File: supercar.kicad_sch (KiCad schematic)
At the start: 41 parts, among them SW1 Power, U1 74HC283, U2 74HC574, U3 74HC154, U4 74HC574, U5 74HC86, U6 NE555D

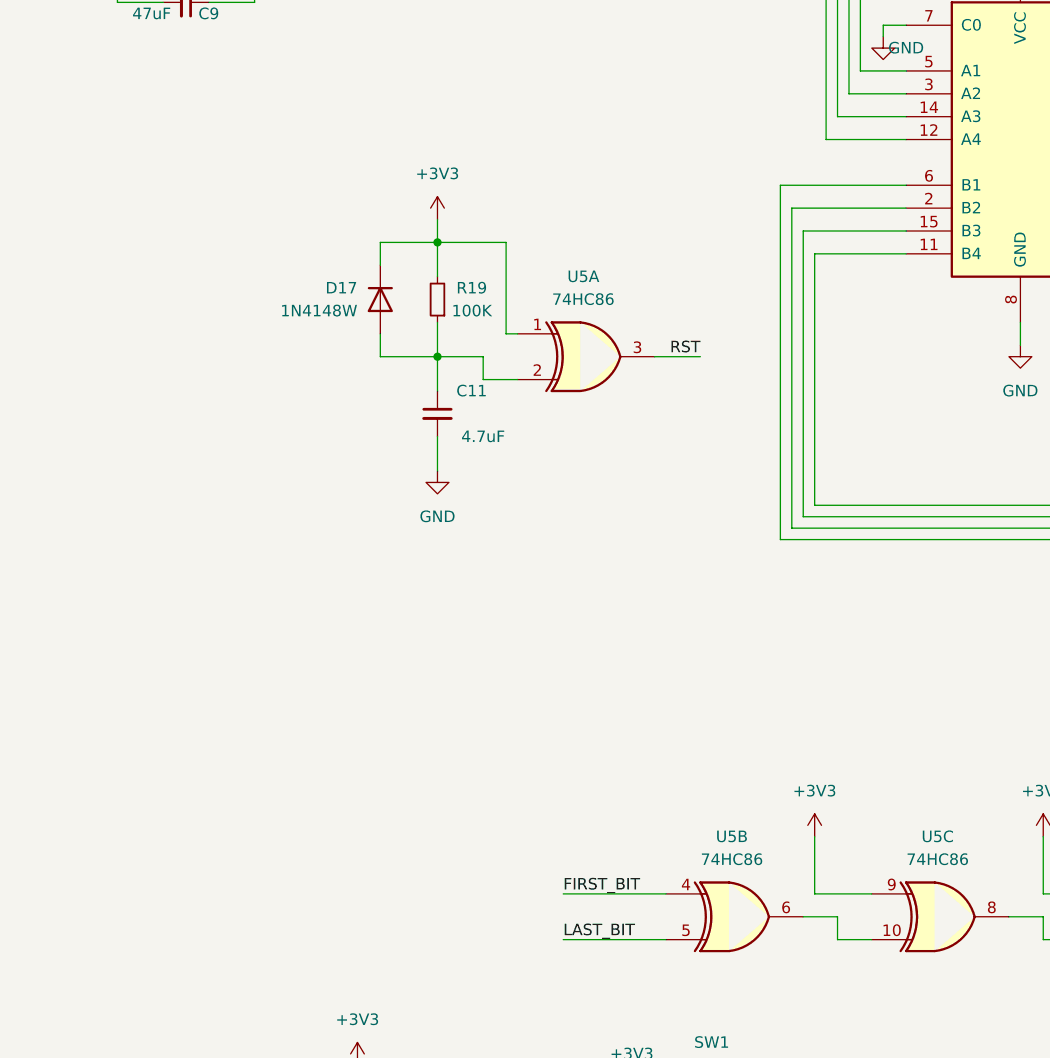
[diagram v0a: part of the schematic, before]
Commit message: Feed the reset circuit on the delay line of the adder clock
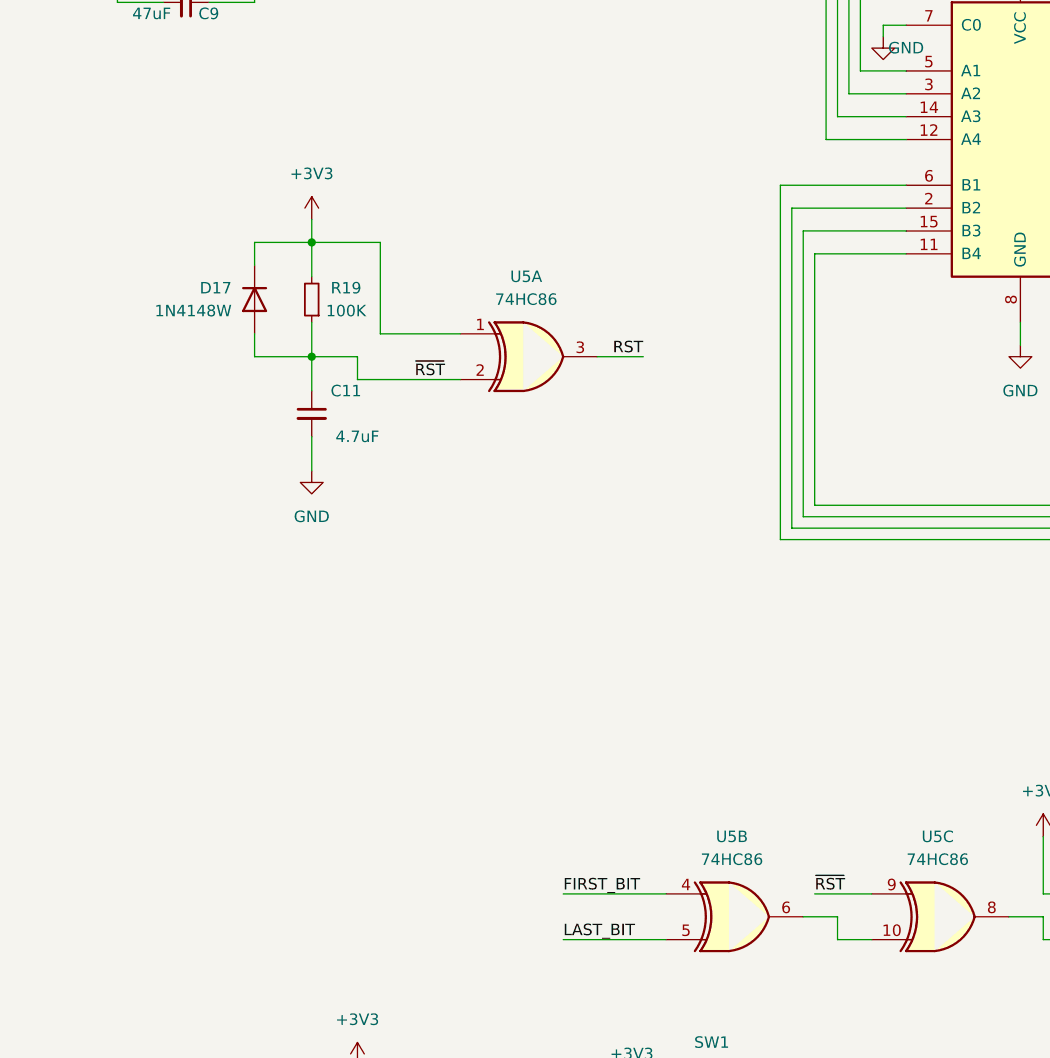
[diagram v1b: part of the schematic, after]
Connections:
- net +3V3: no longer U5.9
- net ~{RST}: now reaches C11.1, D17.2 (A), R19.1, U5.2
- net ~{RST}: now also U5.9
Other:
- moved on the sheet: C11, D17, R19, U5A

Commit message: Fix schematics
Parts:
- SW1: footprint Button_Switch_THT:SW_Slide_1P2T_CK_OS102011MS2Q -> Button_Switch_SMD:SW_SPDT_CK-JS102011SAQN
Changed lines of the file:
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@@
   )
   (symbol (lib_id "Switch:SW_SPDT") (at 90.17 161.29 0) (unit 1)
-    (in_bom yes) (on_board yes) (dnp no) (fields_autoplaced)
+    (in_bom yes) (on_board yes) (dnp no)
     (property "Reference" "SW1" (at 90.17 152.4 0)
       (effects (font (size 1.27 1.27)))
@@
       (effects (font (size 1.27 1.27)))
     )
-    (property "Footprint" "Button_Switch_THT:SW_Slide_1P2T_CK_OS102011MS2Q" (at 90.17 161.29 0)
+    (property "Footprint" "Button_Switch_SMD:SW_SPDT_CK-JS102011SAQN" (at 88.9 167.64 0)
       (effects (font (size 1.27 1.27)) hide)
     )
